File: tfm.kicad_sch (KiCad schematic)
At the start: 34 parts, among them J1 Screw_Terminal_01x04, J2 Screw_Terminal_01x04, J3 Conn_01x03, J4 Conn_01x03, J5 Conn_01x03, J6 Conn_02x04_Counter_Clockwise, U1 LPS25HB, U2 SHT40, U3 NCP1117-3.3_SOT223, U4 HLK-2M05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

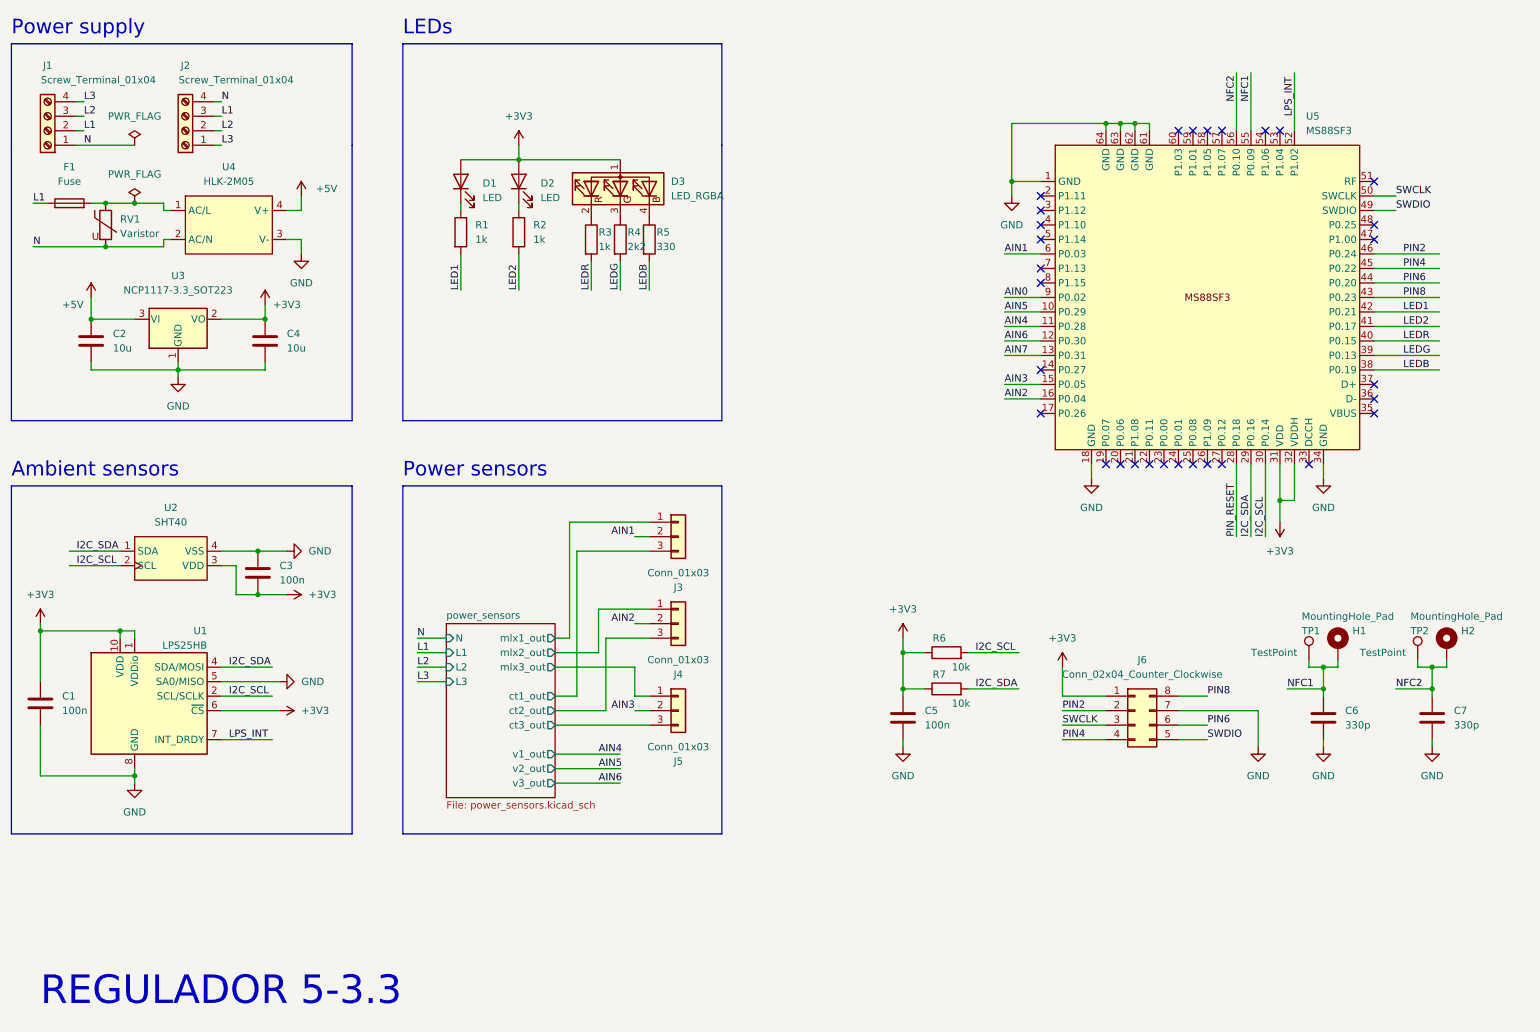
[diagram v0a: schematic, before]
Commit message: Edge cuts with curves
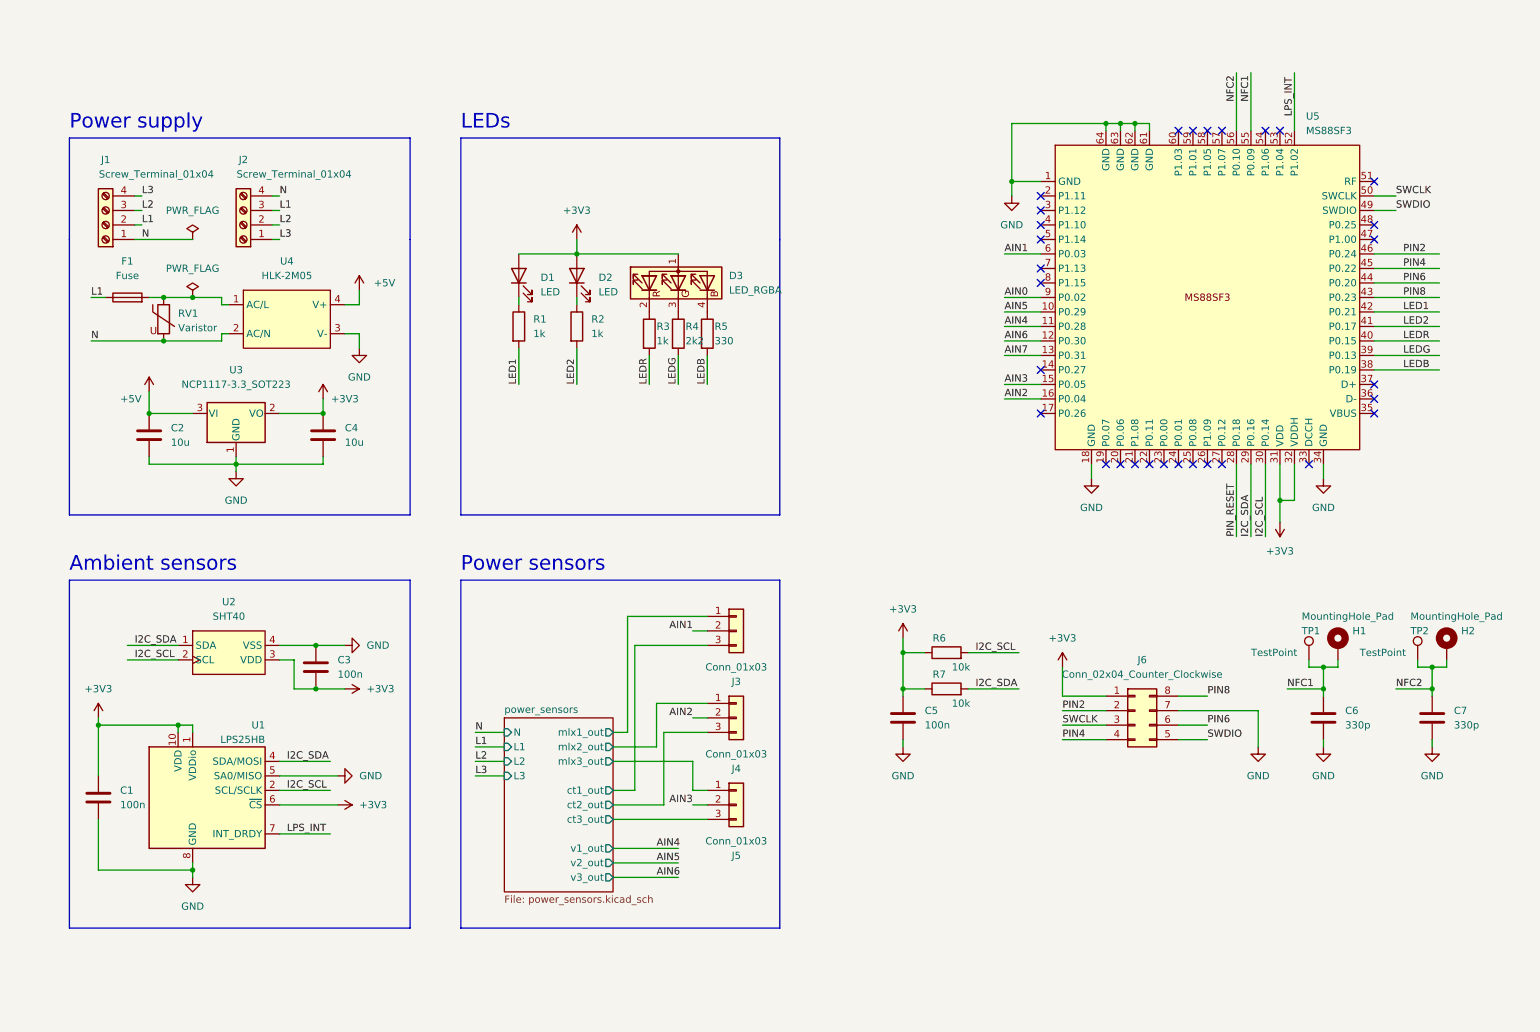
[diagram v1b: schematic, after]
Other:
- note removed: "REGULADOR 5-3.3"
- moved on the sheet: C1, C2, C3, C4, D1, D2, D3, F1, J1, J2, J3, J4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

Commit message: Minor changes
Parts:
- removed H1, H2: MountingHole_Pad, Connector_Pin:Pin_D0.7mm_L6.5mm_W1.8mm_FlatFork, symbol Mechanical:MountingHole_Pad
- added J?: (no value), symbol Connector:Conn_01x02_Female
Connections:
- net NFC1: now also J?.1 (Pin_1)
- net NFC2: now also J?.2 (Pin_2)
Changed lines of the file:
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@@
+    (stroke (width 0) (type default) (color 0 0 0 0))
+  )
+  (wire (pts (xy 270.51 118.11) (xy 270.51 114.3))
     (stroke (width 0) (type default) (color 0 0 0 0))
   )
@@
     (stroke (width 0) (type default) (color 0 0 0 0))
   )
+  (wire (pts (xy 254 129.54) (xy 254 118.11))
+    (stroke (width 0) (type default) (color 0 0 0 0))
+  )
   (wire (pts (xy 196.85 44.45) (xy 196.85 34.29))
     (stroke (width 0) (type default) (color 0 0 0 0))
@@
     (stroke (width 0) (type default) (color 0 0 0 0))
   )
-  (wire (pts (xy 254 129.54) (xy 254 128.27))
-    (stroke (width 0) (type default) (color 0 0 0 0))
-  )
   (wire (pts (xy 127 151.13) (xy 130.81 151.13))
     (stroke (width 0) (type default) (color 0 0 0 0))
   )
-  (wire (pts (xy 273.05 129.54) (xy 273.05 128.27))
+  (wire (pts (xy 273.05 114.3) (xy 273.05 129.54))
     (stroke (width 0) (type default) (color 0 0 0 0))
   )
@@
   )
   (wire (pts (xy 129.54 120.65) (xy 143.51 120.65))
+    (stroke (width 0) (type default) (color 0 0 0 0))
+  )
+  (wire (pts (xy 254 118.11) (xy 270.51 118.11))
     (stroke (width 0) (type default) (color 0 0 0 0))
   )
@@
     (pin "2")
   )
+  (symbol (lib_id "Connector:Conn_01x02_Female") (at 270.51 109.22 90) (unit 1)
+    (in_bom yes) (on_board yes) (fields_autoplaced)
+    (property "Reference" "J?" (id 0) (at 274.32 108.5849 90)
+      (effects (font (size 1.27 1.27)) (justify right))
+    )
+    (property "Value" "" (id 1) (at 274.32 111.1249 90)
+      (effects (font (size 1.27 1.27)) (justify right))
+    )
+    (property "Footprint" "" (id 2) (at 270.51 109.22 0)
+      (effects (font (size 1.27 1.27)) hide)
+    )
+    (property "Datasheet" "~" (id 3) (at 270.51 109.22 0)
+      (effects (font (size 1.27 1.27)) hide)
+    )
+    (pin "1")
+    (pin "2")
+  )
   (symbol (lib_id "power:GND") (at 251.46 96.52 0) (unit 1)
     (in_bom yes) (on_board yes) (fields_autoplaced)
@@
     )
     (property "Datasheet" "" (id 3) (at 80.01 125.73 0)
-      (effects (font (size 1.27 1.27)) hide)
-    )
-    (pin "1")
-  )
-  (symbol (lib_id "Mechanical:MountingHole_Pad") (at 273.05 125.73 0) (unit 1)
-    (in_bom yes) (on_board yes)
-    (property "Reference" "H2" (id 0) (at 275.59 123.1899 0)
-      (effects (font (size 1.27 1.27)) (justify left))
-    )
-    (property "Value" "MountingHole_Pad" (id 1) (at 266.7 120.65 0)
-      (effects (font (size 1.27 1.27)) (justify left))
-    )
-    (property "Footprint" "Connector_Pin:Pin_D0.7mm_L6.5mm_W1.8mm_FlatFork" (id 2) (at 273.05 125.73 0)
-      (effects (font (size 1.27 1.27)) hide)
-    )
-    (property "Datasheet" "~" (id 3) (at 273.05 125.73 0)
       (effects (font (size 1.27 1.27)) hide)
     )
@@
     (pin "1")
     (pin "2")
-  )
-  (symbol (lib_id "Mechanical:MountingHole_Pad") (at 254 125.73 0) (unit 1)
-    (in_bom yes) (on_board yes)
-    (property "Reference" "H1" (id 0) (at 256.54 123.1899 0)
-      (effects (font (size 1.27 1.27)) (justify left))
-    )
-    (property "Value" "MountingHole_Pad" (id 1) (at 247.65 120.65 0)
-      (effects (font (size 1.27 1.27)) (justify left))
-    )
-    (property "Footprint" "Connector_Pin:Pin_D0.7mm_L6.5mm_W1.8mm_FlatFork" (id 2) (at 254 125.73 0)
-      (effects (font (size 1.27 1.27)) hide)
-    )
-    (property "Datasheet" "~" (id 3) (at 254 125.73 0)
-      (effects (font (size 1.27 1.27)) hide)
-    )
-    (pin "1")
   )
   (symbol (lib_id "Device:R") (at 185.42 127 90) (unit 1)
@@
       (reference "F1") (unit 1) (value "Fuse") (footprint "Fuse:Fuse_2512_6332Metric")
     )
-    (path "/db00ed9d-5cbd-42e1-a367-f32e41a8348a"
-      (reference "H1") (unit 1) (value "MountingHole_Pad") (footprint "Connector_Pin:Pin_D0.7mm_L6.5mm_W1.8mm_FlatFork")
-    )
-    (path "/7023e80b-5dcd-4c99-b211-bda07ca1e029"
-      (reference "H2") (unit 1) (value "MountingHole_Pad") (footprint "Connector_Pin:Pin_D0.7mm_L6.5mm_W1.8mm_FlatFork")
-    )
     (path "/89ca5dbf-ffcd-4580-a3a6-e1aae7fb38ca"
       (reference "J1") (unit 1) (value "Screw_Terminal_01x04") (footprint "guille_3rdparty:TerminalBlock_Altech_AK300-4_P5.00mm")
@@
       (reference "J6") (unit 1) (value "Conn_02x04_Counter_Clockwise") (footprint "Connector_PinSocket_1.27mm:PinSocket_2x04_P1.27mm_Vertical_SMD")
     )
+    (path "/4ee0ea3c-39fa-4305-9302-2ee36fb0816a"
+      (reference "J?") (unit 1) (value "Conn_01x02_Female") (footprint "")
+    )
     (path "/5fe5f375-4e42-4c76-a2a1-ff8c6cf7ef08"

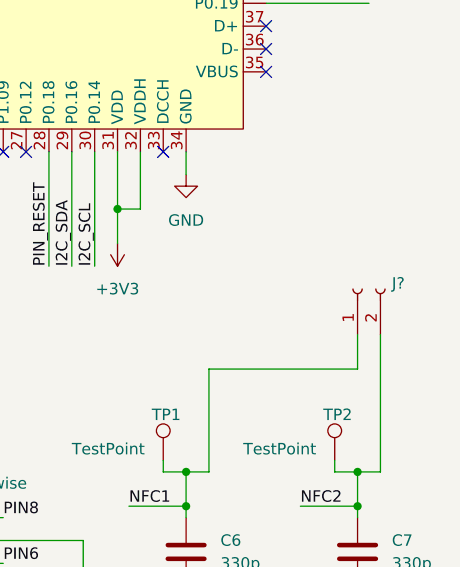
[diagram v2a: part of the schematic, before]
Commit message: Uodate schematic with NFC header
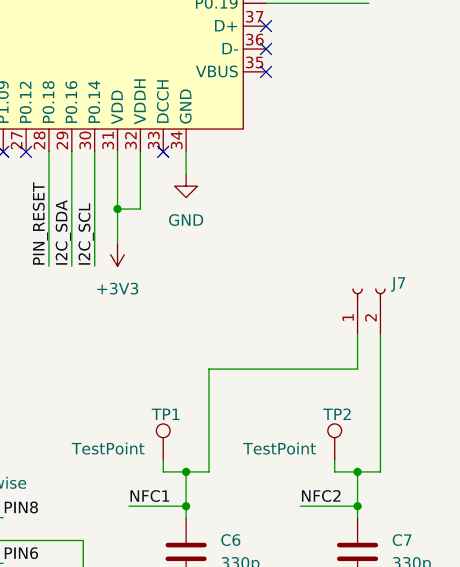
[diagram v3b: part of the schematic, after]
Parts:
- gave numbers to parts that had none: 1
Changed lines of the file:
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@@
   (symbol (lib_id "Connector:Conn_01x02_Female") (at 270.51 109.22 90) (unit 1)
     (in_bom yes) (on_board yes) (fields_autoplaced)
-    (property "Reference" "J?" (id 0) (at 274.32 108.5849 90)
+    (property "Reference" "J7" (id 0) (at 274.32 108.5849 90)
       (effects (font (size 1.27 1.27)) (justify right))
     )
@@
     )
     (path "/4ee0ea3c-39fa-4305-9302-2ee36fb0816a"
-      (reference "J?") (unit 1) (value "Conn_01x02_Female") (footprint "")
+      (reference "J7") (unit 1) (value "Conn_01x02_Female") (footprint "Connector_PinHeader_2.54mm:PinHeader_1x02_P2.54mm_Vertical")
     )
     (path "/5fe5f375-4e42-4c76-a2a1-ff8c6cf7ef08"

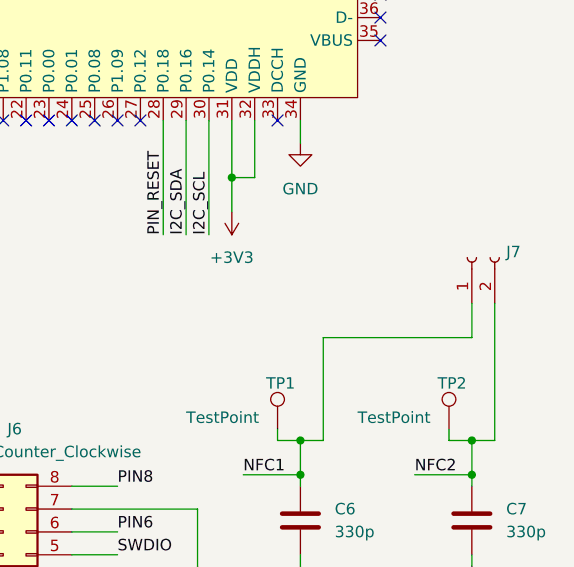
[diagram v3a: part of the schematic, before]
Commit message: Change libraries path
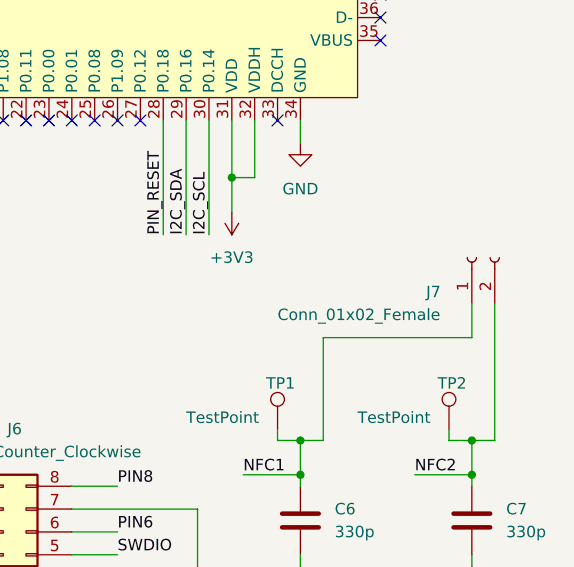
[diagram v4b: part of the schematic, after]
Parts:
- J7: value (none) -> Conn_01x02_Female; footprint (none) -> Connector_PinHeader_2.54mm:PinHeader_1x02_P2.54mm_Vertical
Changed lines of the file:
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@@
   )
   (symbol (lib_id "Connector:Conn_01x02_Female") (at 270.51 109.22 90) (unit 1)
-    (in_bom yes) (on_board yes) (fields_autoplaced)
-    (property "Reference" "J7" (id 0) (at 274.32 108.5849 90)
+    (in_bom yes) (on_board yes)
+    (property "Reference" "J7" (id 0) (at 265.43 113.03 90)
       (effects (font (size 1.27 1.27)) (justify right))
     )
-    (property "Value" "" (id 1) (at 274.32 111.1249 90)
+    (property "Value" "Conn_01x02_Female" (id 1) (at 248.92 115.57 90)
       (effects (font (size 1.27 1.27)) (justify right))
     )
-    (property "Footprint" "" (id 2) (at 270.51 109.22 0)
+    (property "Footprint" "Connector_PinHeader_2.54mm:PinHeader_1x02_P2.54mm_Vertical" (id 2) (at 270.51 109.22 0)
       (effects (font (size 1.27 1.27)) hide)
     )

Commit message: Update 3d references and add testpoints
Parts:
- F1: value Fuse -> (none); footprint Fuse:Fuse_2512_6332Metric -> (none)
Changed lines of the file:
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@@
     (in_bom yes) (on_board yes) (fields_autoplaced)
     (property "Reference" "F1" (id 0) (at 41.91 58.42 90))
-    (property "Value" "Fuse" (id 1) (at 41.91 60.96 90))
-    (property "Footprint" "Fuse:Fuse_2512_6332Metric" (id 2) (at 41.91 66.548 90)
+    (property "Value" "" (id 1) (at 41.91 60.96 90))
+    (property "Footprint" "" (id 2) (at 41.91 66.548 90)
       (effects (font (size 1.27 1.27)) hide)
     )
@@
     )
     (path "/89cc9ca6-9bb9-4622-9549-65a2508f1be8"
-      (reference "F1") (unit 1) (value "Fuse") (footprint "Fuse:Fuse_2512_6332Metric")
+      (reference "F1") (unit 1) (value "Fuse") (footprint "guille_3rdparty:Fuse_2512_6332Metric")
     )
     (path "/89ca5dbf-ffcd-4580-a3a6-e1aae7fb38ca"
@@
       (reference "TP2") (unit 1) (value "TestPoint") (footprint "TestPoint:TestPoint_Pad_D1.5mm")
     )
+    (path "/62a1ccba-28df-479f-b158-915abf26b93e/980a11d8-19d4-4758-8a8c-2941d0c040bc"
+      (reference "TP3") (unit 1) (value "TestPoint") (footprint "TestPoint:TestPoint_Pad_D1.5mm")
+    )
+    (path "/62a1ccba-28df-479f-b158-915abf26b93e/4a443588-6a1d-408e-a939-f58fed09f5ca"
+      (reference "TP4") (unit 1) (value "TestPoint") (footprint "TestPoint:TestPoint_Pad_D1.5mm")
+    )
+    (path "/62a1ccba-28df-479f-b158-915abf26b93e/5b681c77-25ce-49d8-bdaf-e79a091e461e"
+      (reference "TP5") (unit 1) (value "TestPoint") (footprint "TestPoint:TestPoint_Pad_D1.5mm")
+    )
+    (path "/62a1ccba-28df-479f-b158-915abf26b93e/82b2636f-d6be-4fdd-99d3-3acb0391665a"
+      (reference "TP6") (unit 1) (value "TestPoint") (footprint "TestPoint:TestPoint_Pad_D1.5mm")
+    )
+    (path "/62a1ccba-28df-479f-b158-915abf26b93e/d92c4cae-d7a9-48b8-a66c-89761540cf50"
+      (reference "TP7") (unit 1) (value "TestPoint") (footprint "TestPoint:TestPoint_Pad_D1.5mm")
+    )
+    (path "/62a1ccba-28df-479f-b158-915abf26b93e/a106b65c-2dce-4edb-95fa-092ebe4135ce"
+      (reference "TP8") (unit 1) (value "TestPoint") (footprint "TestPoint:TestPoint_Pad_D1.5mm")
+    )
+    (path "/62a1ccba-28df-479f-b158-915abf26b93e/2a419547-fbe1-4e45-892d-f306410f3c9d"
+      (reference "TP9") (unit 1) (value "TestPoint") (footprint "TestPoint:TestPoint_Pad_D1.5mm")
+    )
     (path "/366beb35-98dc-4b97-8c7f-596e44284f35"

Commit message: Add decoupling capacitors, expansion port and test ponits
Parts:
- added J6: (no value), symbol Connector:Conn_01x04_Male
- added TP1, TP2: (no value), symbol Connector:TestPoint
- C2: value 10u -> (none); footprint Capacitor_SMD:C_0402_1005Metric -> (none)
- C4: footprint Capacitor_SMD:C_0402_1005Metric -> (none)
- F1: value (none) -> Fuse; footprint (none) -> guille_3rdparty:Fuse_2512_6332Metric
- renumbered J6 to J7, J7 to J8, TP1 to TP3, TP2 to TP4
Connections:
- net +3V3: now also J6.1 (Pin_1)
- net GND: now also J6.4 (Pin_4)
- net I2C_SCL: now also TP1.1
- net I2C_SDA: now also TP2.1
- net EXT2: now reaches U5.19 (P0.07)
- net EXT2: now also J6.3 (Pin_3)
- net EXT1: now reaches U5.20 (P0.06)
- net EXT1: now also J6.2 (Pin_2)
- net AIN0: no longer names the net of U5.9 (P0.02)
- net AIN7: no longer names the net of U5.13 (P0.31)
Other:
- moved on the sheet: R6
